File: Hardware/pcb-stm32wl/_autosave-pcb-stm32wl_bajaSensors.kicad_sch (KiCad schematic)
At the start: 0 parts

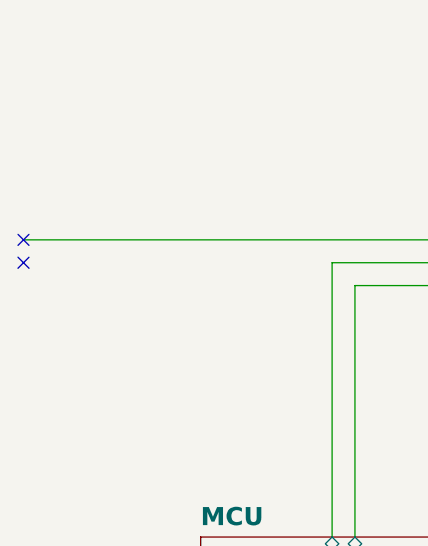
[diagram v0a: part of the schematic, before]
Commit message: rewried circuit to account ofr small details
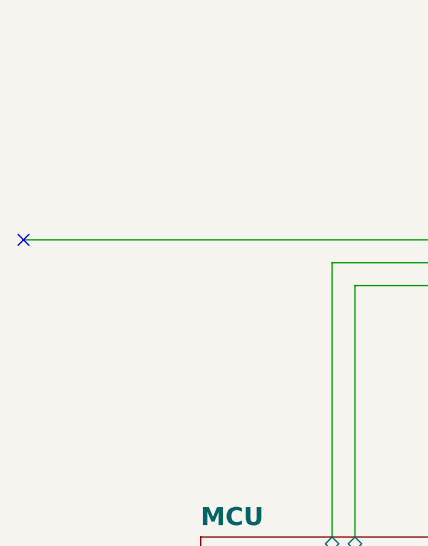
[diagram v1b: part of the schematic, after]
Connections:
- no-connect marks 2 -> 1
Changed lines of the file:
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@@
-	)
-	(no_connect
-		(at 77.47 40.64)
 	)
 	(no_connect
